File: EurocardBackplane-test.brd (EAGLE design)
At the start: 134.6 x 129.8 mm, 10 parts, among them IC1 LM399H, U1 MIC5209, U2 MIC5209, X1 FAC64S, X2 FAC64S

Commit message: Mostly-routed test board with teensy, WIZNET, and vref.
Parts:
- removed U2: MIC5209, regulator-jqi:TO263-5
- removed X1, X2: FAC64S, Eurocard-Backplane-jqi:FAC64S
- added C1, C4, C5, C6: 1uF, jqi_passives:C_MLCC_0603
- added J1: JUMPER, Eurocard-Backplane-jqi:JUMP
- added R3, R4: (no value), jqi_passives:R_0603
- added R5: 7.5k, jqi_passives:R_0603
- added TEENSY: TEENSY_3.1_ALL_PINS_AND_PADS, mcu-accessories:TEENSY_3.1_ALLPINS
- added U$1: (no value), JQI_Logo:JQI_LOGO_NEGATIVE-SILKSCREEN
- added U3: MIC5209-3.3YS, regulator-jqi:SOT223-S
- added X5, X6, X7_AUX: FAC64S, Eurocard-Backplane-jqi:FAC64S
- U$4: value TEENSY_3.1_ALL_PINS_AND_PADS -> (none); device mcu-accessories:TEENSY_3.1_ALLPINS -> JQI_Logo:JQI_LOGO_NEGATIVE-SILKSCREEN
- moved U1 295.6 mm to (167.6, 87.4)
- moved IC1 229.9 mm to (104.1, 26.7), turned to 90 degrees
- moved U$2 197.8 mm to (118.1, 53.3)
- moved JP2 192.0 mm to (101.6, 94.0)
- moved U$4 99.6 mm to (11.9, 110.2), flipped to the bottom, turned to 0 degrees
- moved X3 43.0 mm to (119.9, 22.6), turned to 270 degrees
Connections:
- removed net AGND: U$4.AGND
- removed net HV_INTERLOCK1: X2.A25, X2.C25
- removed net I2C_SCL1: X2.C14
- removed net I2C_SDA1: X2.A14
- removed net N$2: X2.C11
- removed net N$23: X1.A30, X1.C30
- removed net N$24: X1.A32, X1.C32
- removed net N$25: X1.A26, X1.C26
- removed net N$26: X1.A27, X1.C27
- removed net N$3: X2.A10
- removed net SPI_CS: X1.C12
- removed net SPI_CS1: X2.C12
- removed net SPI_MISO1: X2.C13
- removed net SPI_MOSI1: X2.A13
- removed net SPI_SCLK1: X2.A12
- new net -15V: X3.1, X5.A30, X5.C30, X6.A30, X6.C30, X7_AUX.A30, X7_AUX.C30
- new net 3.3V: TEENSY.3.3V, TEENSY.3.3V1, TEENSY.3.3V2
- new net A15: X5.A15, X6.A15, X7_AUX.A15
- new net A16: X5.A16, X6.A16, X7_AUX.A16
- new net A17: X5.A17, X6.A17, X7_AUX.A17
- new net A18: X5.A18, X6.A18, X7_AUX.A18
- new net A19: X5.A19, X6.A19, X7_AUX.A19
- new net A2: X5.A2, X6.A2, X7_AUX.A2
- new net A20: X5.A20, X6.A20, X7_AUX.A20
- new net A21: X5.A21, X6.A21, X7_AUX.A21
- new net A22: X5.A22, X6.A22, X7_AUX.A22
- new net A23: X5.A23, X6.A23, X7_AUX.A23
- new net A27: X5.A27, X6.A27, X7_AUX.A27
- new net A28: X5.A28, X6.A28, X7_AUX.A28
- new net A29: X5.A29, X6.A29, X7_AUX.A29
- new net A5: X5.A5, X6.A5, X7_AUX.A5
- new net A8: X5.A8, X6.A8, X7_AUX.A8
- new net A9: X5.A9, X6.A9, X7_AUX.A9
- new net C15: X5.C15, X6.C15, X7_AUX.C15
- new net C16: X5.C16, X6.C16, X7_AUX.C16
- new net C17: X5.C17, X6.C17, X7_AUX.C17
- new net C18: X5.C18, X6.C18, X7_AUX.C18
- new net C19: X5.C19, X6.C19, X7_AUX.C19
- new net C2: X5.C2, X6.C2, X7_AUX.C2
- new net C20: X5.C20, X6.C20, X7_AUX.C20
- new net C21: X5.C21, X6.C21, X7_AUX.C21
- new net C22: X5.C22, X6.C22, X7_AUX.C22
- new net C23: X5.C23, X6.C23, X7_AUX.C23
- new net C27: X5.C27, X6.C27, X7_AUX.C27
- new net C28: X5.C28, X6.C28, X7_AUX.C28
- new net C29: X5.C29, X6.C29, X7_AUX.C29
- new net C5: X5.C5, X6.C5, X7_AUX.C5
- new net C8: X5.C8, X6.C8, X7_AUX.C8
- new net C9: X5.C9, X6.C9, X7_AUX.C9
- new net HV: X5.A26, X5.C26, X6.A26, X6.C26, X7_AUX.A26, X7_AUX.C26
- new net N$10: TEENSY.32
- new net N$11: TEENSY.31
- new net N$9: TEENSY.30
- new net SPI_CS5: TEENSY.25, X5.C12
- new net SPI_CS6: TEENSY.24, X6.C12
- new net SPI_CS7_AUX: TEENSY.33, X7_AUX.C12
- new net VREF: IC1.1, R5.P$1, X5.A32, X5.C32, X6.A32, X6.C32, X7_AUX.A32, X7_AUX.C32
- net +15V: now also C4.P$2, IC1.3, R5.P$2, U1.1, U1.2, X3.2, X5.A31, X5.C31, X6.A31, X6.C31, X7_AUX.A31, X7_AUX.C31; no longer U2.1, U2.2, X1.A31, X1.C31, X2.A31, X2.C31
- net +3V3: now also C5.P$2, U3.3; no longer U$4.3.3V, U$4.3.3V1, U$4.3.3V2
- net AREF: now also TEENSY.AREF; no longer U$4.AREF
- net D0: now also TEENSY.4, X5.A10, X6.A10, X7_AUX.A10; no longer U$4.4, X1.A10
- net D1: now also TEENSY.1, X5.C10, X6.C10, X7_AUX.C10; no longer U$4.1, X1.C10
- net D2: now also TEENSY.3, X5.A11, X6.A11, X7_AUX.A11; no longer U$4.3, X1.A11
- net D3: now also TEENSY.0, X5.C11, X6.C11, X7_AUX.C11; no longer U$4.0, X1.C11
- net GND: now also IC1.2, IC1.4, J1.P$2, TEENSY.AGND, X3.3, X3.4, X5.A1, X5.A25, X5.C1, X5.C25, X6.A1, X6.A25, X6.C1, X6.C25, X7_AUX.A1, X7_AUX.A25, X7_AUX.C1, X7_AUX.C25; no longer X1.A1, X1.C1, X2.A1, X2.C1
- net GPIO#0: now also TEENSY.A14; no longer U$4.A14
- net GPIO#1: now also TEENSY.22/A8; no longer U$4.14/A0
- net GPIO#2: now also TEENSY.21/A7; no longer U$4.15/A1
- net GPIO#3: now also TEENSY.20/A6; no longer U$4.16/A2
- net GPIO#4: now also TEENSY.17/A3; no longer U$4.17/A3
- net GPIO#5: now also TEENSY.16/A2; no longer U$4.20/A6
- net GPIO#6: now also TEENSY.15/A1; no longer U$4.21/A7
- net GPIO#7: now also TEENSY.14/A0; no longer U$4.22/A8
- net GPIO0: now also X5.A3, X6.A3, X7_AUX.A3; no longer X1.A3, X2.A3
- net GPIO1: now also X5.C3, X6.C3, X7_AUX.C3; no longer X1.C3, X2.C3
- net GPIO2: now also X5.A4, X6.A4, X7_AUX.A4; no longer X1.A4, X2.A4
- net GPIO3: now also X5.C4, X6.C4, X7_AUX.C4; no longer X1.C4, X2.C4
- net GPIO4: now also X5.A6, X6.A6, X7_AUX.A6; no longer X1.A6, X2.A6
- net GPIO5: now also X5.C6, X6.C6, X7_AUX.C6; no longer X1.C6, X2.C6
- net GPIO6: now also X5.A7, X6.A7, X7_AUX.A7; no longer X1.A7, X2.A7
- net GPIO7: now also X5.C7, X6.C7, X7_AUX.C7; no longer X1.C7, X2.C7
- net HV_INTERLOCK: now also TEENSY.6, X5.A24, X5.C24, X6.A24, X6.C24, X7_AUX.A24, X7_AUX.C24; no longer U$4.6, X1.A25, X1.C25
- net I2C_SCL: now also TEENSY.19/A5, X5.C14, X6.C14, X7_AUX.C14; no longer U$4.19/A5, X1.C14
- net I2C_SDA: now also TEENSY.18/A4, X5.A14, X6.A14, X7_AUX.A14; no longer U$4.18/A4, X1.A14
- net N$1: now also TEENSY.23/A9; no longer X2.C10
- net N$4: now also TEENSY.26; no longer X2.A11
- net N$5: now also R3.P$1, R4.P$2, U1.5; no longer X2.A30, X2.C30
- net N$6: now also TEENSY.27; no longer X2.A32, X2.C32
- net N$7: now also TEENSY.28; no longer X2.A26, X2.C26
- net N$8: now also TEENSY.29; no longer X2.A27, X2.C27
- net SPI_MISO: now also TEENSY.12, X5.C13, X6.C13, X7_AUX.C13; no longer U$4.12, X1.C13
- net SPI_MOSI: now also TEENSY.11, X5.A13, X6.A13, X7_AUX.A13; no longer U$4.11, X1.A13
- net SPI_SCLK: now also TEENSY.13, X5.A12, X6.A12, X7_AUX.A12; no longer U$4.13, X1.A12
- net VBAT: now also TEENSY.VBAT; no longer U$4.VBAT
- net VDD: now also C1.P$2, C6.P$2, R3.P$2, TEENSY.VIN, U1.4, U3.1; no longer U$4.VIN
- net VSS: now also C1.P$1, C4.P$1, C5.P$1, C6.P$1, J1.P$1, R4.P$1, TEENSY.GND, TEENSY.GND1, TEENSY.GND2, U1.3, U1.6, U3.2, U3.4; no longer U$4.GND, U$4.GND1, U$4.GND2
- net VUSB: now also TEENSY.VUSB; no longer U$4.VUSB
- net WIZNET_INTERRUPT: now also TEENSY.8; no longer U$4.8
- net WIZNET_PWDN: now also TEENSY.9; no longer U$4.9
- net WIZNET_RESET: now also TEENSY.7; no longer U$4.7
- net WIZNET_SS: now also TEENSY.10; no longer U$4.10
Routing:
- net SPI_MISO: track 0.00 -> 131.5 mm
- net I2C_SCL: track 0.00 -> 106.9 mm
- net I2C_SDA: track 0.00 -> 106.3 mm
- net SPI_MOSI: track 0.00 -> 104.0 mm
- net VREF: track 0.00 -> 83.9 mm
- net D2: track 0.00 -> 74.5 mm
- net D0: track 0.00 -> 72.1 mm
- net SPI_SCLK: track 35.5 -> 105.6 mm
- net D3: track 0.00 -> 69.1 mm
- net C5: track 0.00 -> 66.5 mm
- net C16: track 0.00 -> 66.5 mm
- net C9: track 0.00 -> 66.5 mm
- net C2: track 0.00 -> 66.5 mm
- net C23: track 0.00 -> 66.5 mm
- net C22: track 0.00 -> 66.5 mm
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- added copper zone on layer 15, net +15V
- added copper zone on layer 2, net -15V
- added copper zone on layer 15, net GND
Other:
- board text added: "HV"

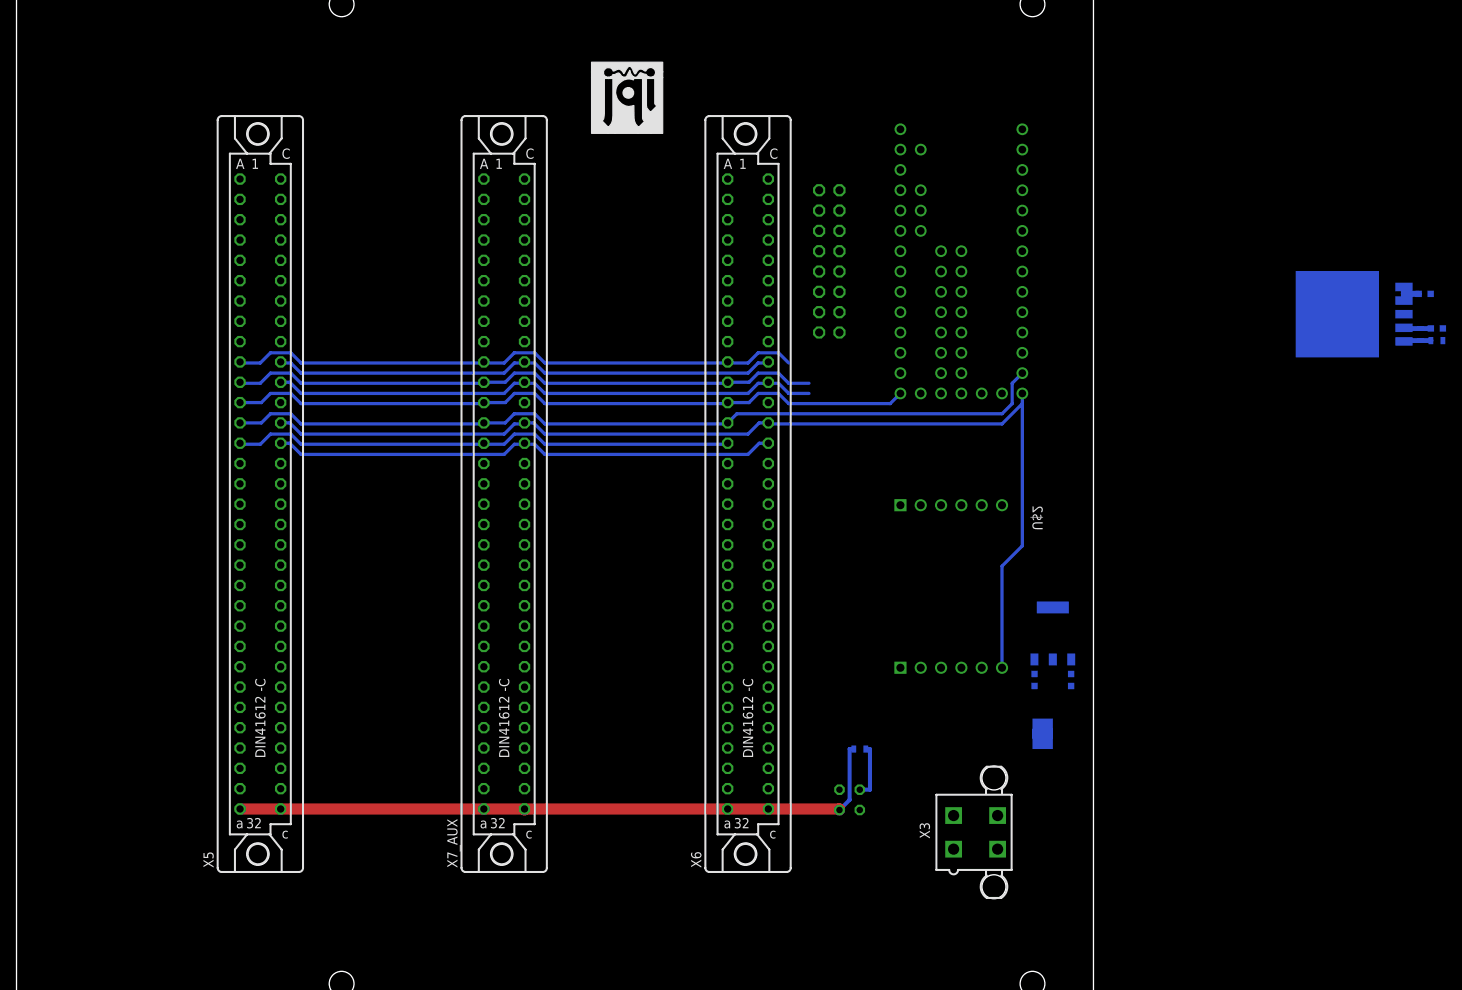
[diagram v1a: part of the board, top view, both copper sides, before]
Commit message: routing and layout of test board done
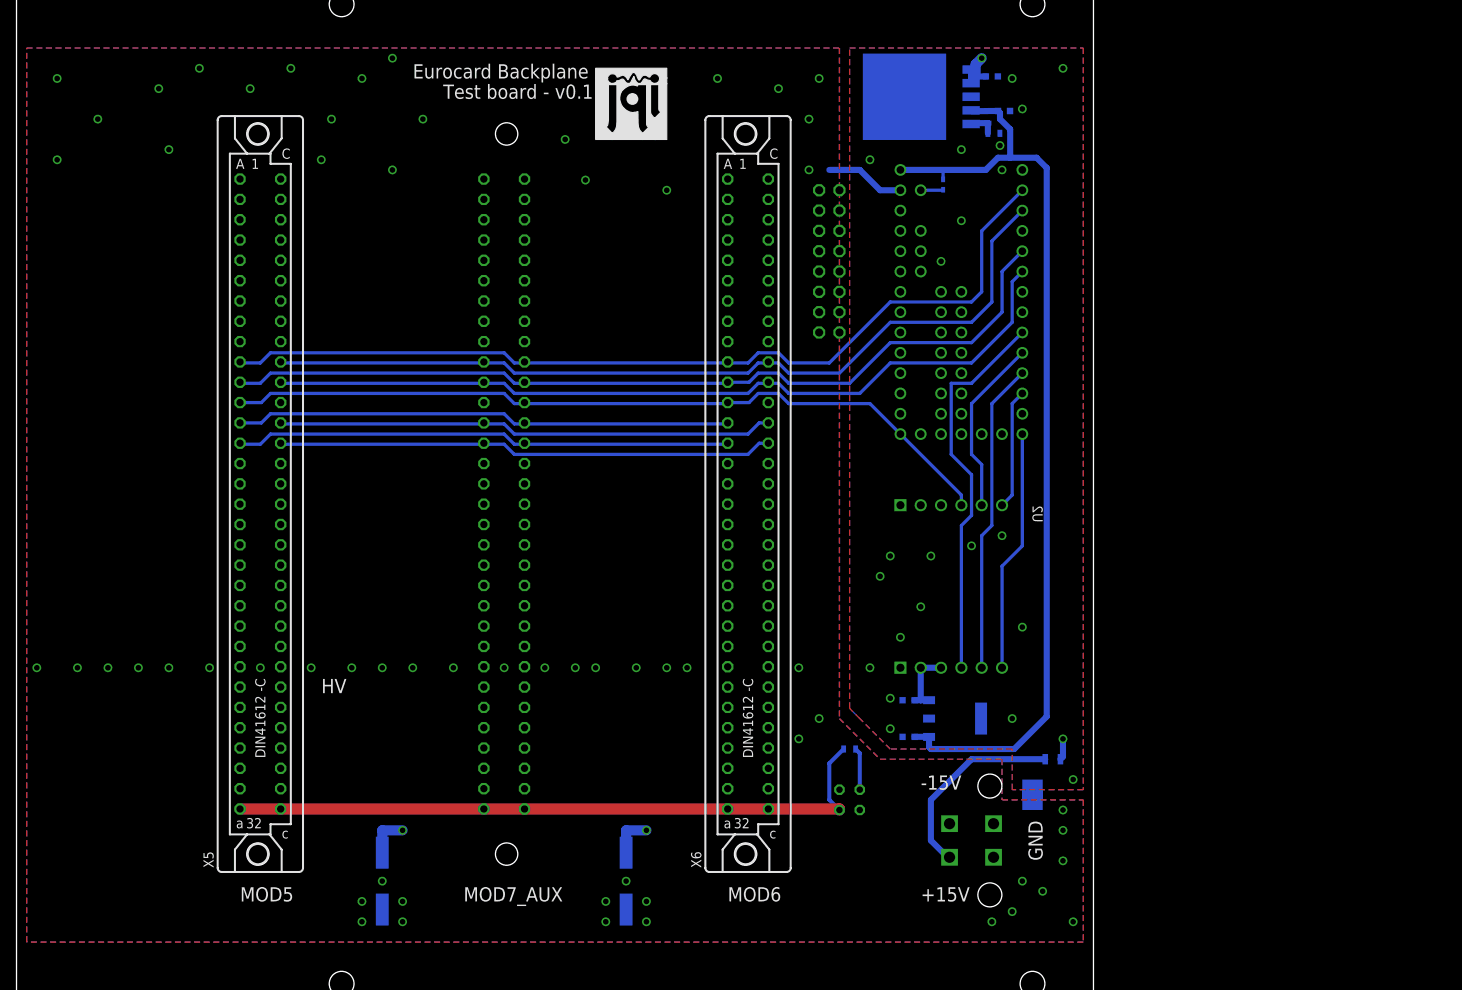
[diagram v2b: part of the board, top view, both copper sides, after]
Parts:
- added C2, C3: (no value), jqi_passives:PANASONIC_F
- added D1: (no value), diode:SOD523
- added L1: (no value), jqi_passives:R_0805
- moved U$4 69.3 mm to (81.3, 109.2)
- moved R4 61.1 mm to (122.2, 110.0)
- moved R3 60.5 mm to (121.4, 112.0)
- moved C1 60.5 mm to (123.4, 112.8)
- moved C4 60.5 mm to (121.9, 117.1)
- moved U1 60.5 mm to (113.5, 114.6)
- moved C6 21.5 mm to (111.5, 34.5), turned to 180 degrees
- moved U3 16.6 mm to (115.6, 36.8), turned to 90 degrees
- moved C5 16.0 mm to (111.5, 39.1), turned to 180 degrees
- moved J1 7.73 mm to (127.0, 26.7)
- moved TEENSY 5.08 mm to (118.1, 87.6)
- moved R5 1.27 mm to (104.1, 33.0)
- moved X3 1.14 mm to (119.4, 21.6), flipped to the bottom, turned to 90 degrees
- moved U$1 0.92 mm to (72.4, 109.2)
- flipped X7_AUX to the bottom
- renumbered U$2 to U2
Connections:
- net N$11 renamed SPI_CS4
- net N$6 renamed SPI_C0
- net N$7 renamed SPI_CS1
- net N$8 renamed SPI_CS2
- net N$9 renamed SPI_CS3
- removed net N$10: TEENSY.32
- removed net N$4: TEENSY.26
- removed net VUSB: TEENSY.VUSB
- new net N$2: D1.A, TEENSY.VUSB
- net +15V: now also C2.+, L1.P$1; no longer C4.P$2, U1.1, U1.2
- net -15V: now also C3.-
- net D0: now also TEENSY.0; no longer TEENSY.4
- net D3: now also TEENSY.4; no longer TEENSY.0
- net GND: now also C2.-, C3.+
- net N$1: now also C4.P$2, L1.P$2, U1.1, U1.2; no longer TEENSY.23/A9
- net SPI_CS5: now also TEENSY.32; no longer TEENSY.25
- net SPI_CS6: now also TEENSY.33; no longer TEENSY.24
- net SPI_CS7_AUX: now also TEENSY.25; no longer TEENSY.33
- net VDD: now also D1.C
- net WIZNET_INTERRUPT: now also TEENSY.10; no longer TEENSY.8
- net WIZNET_PWDN: now also TEENSY.7; no longer TEENSY.9
- net WIZNET_RESET: now also TEENSY.9; no longer TEENSY.7
- net WIZNET_SS: now also TEENSY.8; no longer TEENSY.10
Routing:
- net VDD: track 3.47 -> 118.7 mm
- net N$1: track 0.00 -> 101.7 mm, vias 0 -> 2
- net SPI_CS5: track 0.00 -> 99.0 mm
- net SPI_CS7_AUX: track 0.00 -> 79.6 mm
- net HV_INTERLOCK: track 66.0 -> 136.2 mm
- net GND: track 66.3 -> 10.1 mm, vias 0 -> 62
- net SPI_C0: track 0.00 -> 53.8 mm
- net WIZNET_PWDN: track 0.00 -> 48.7 mm
- net D1: track 63.5 -> 107.6 mm
- net SPI_CS1: track 0.00 -> 44.0 mm
- net D0: track 72.1 -> 113.6 mm
- net SPI_CS4: track 0.00 -> 41.1 mm
- net SPI_CS3: track 0.00 -> 40.4 mm
- net SPI_CS2: track 0.00 -> 40.4 mm
- net WIZNET_RESET: track 0.00 -> 38.9 mm
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- added copper zone on layer 2, net +15V
- added copper zone on layer 15, net -15V
- added copper zone on layer 1, net GND
- added copper zone on layer 16, net GND
- added copper zone on layer 2, net GND
- added copper zone on layer 1, net VSS
- added copper zone on layer 15, net VSS
- added copper zone on layer 16, net VSS
- added copper zone on layer 2, net VSS
- removed copper zone on layer 15, net +15V
- removed copper zone on layer 2, net -15V
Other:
- board text added: "+15V"
- board text added: "-15V"
- board text added: "Eurocard Backplane"
- board text added: "GND"
- board text added: "MOD5"
- board text added: "MOD6"
- board text added: "MOD7_AUX"
- board text added: "Test board - v0.1"
